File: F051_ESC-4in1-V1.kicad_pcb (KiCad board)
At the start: 4 copper layers, 46 x 49.5 mm, 204 parts, among them J1 Conn_01x02, J11 Conn_01x03, J14 Conn_01x03, J2 Conn_01x10, J3 Conn_01x05, J4 Conn_01x05, J5 Conn_01x05, J6 Conn_01x03, J7 Conn_01x05, J8 Conn_01x03, Q1 TPHR8504PL, Q10 TPHR8504PL, Q11 TPHR8504PL, Q12 TPHR8504PL, Q13 TPHR8504PL, Q14 TPHR8504PL, Q15 TPHR8504PL, Q16 TPHR8504PL, Q17 TPHR8504PL, Q18 TPHR8504PL, Q19 TPHR8504PL, Q2 TPHR8504PL, Q20 TPHR8504PL, Q21 TPHR8504PL, Q22 TPHR8504PL, Q23 TPHR8504PL, Q24 TPHR8504PL, Q3 TPHR8504PL, Q4 TPHR8504PL, Q5 TPHR8504PL, Q6 TPHR8504PL, Q7 TPHR8504PL, Q8 TPHR8504PL, Q9 TPHR8504PL, U1 STM32F051K6Ux, U10 FD6288Q, U11 STM32F051K6Ux, U12 FD6288Q, U2 FD6288Q, U3 L78L12_SOT89, U4 LP2985-3.3, U5 INA139, U6 FD6288Q, U7 OPA340NA, U8 STM32F051K6Ux, U9 STM32F051K6Ux

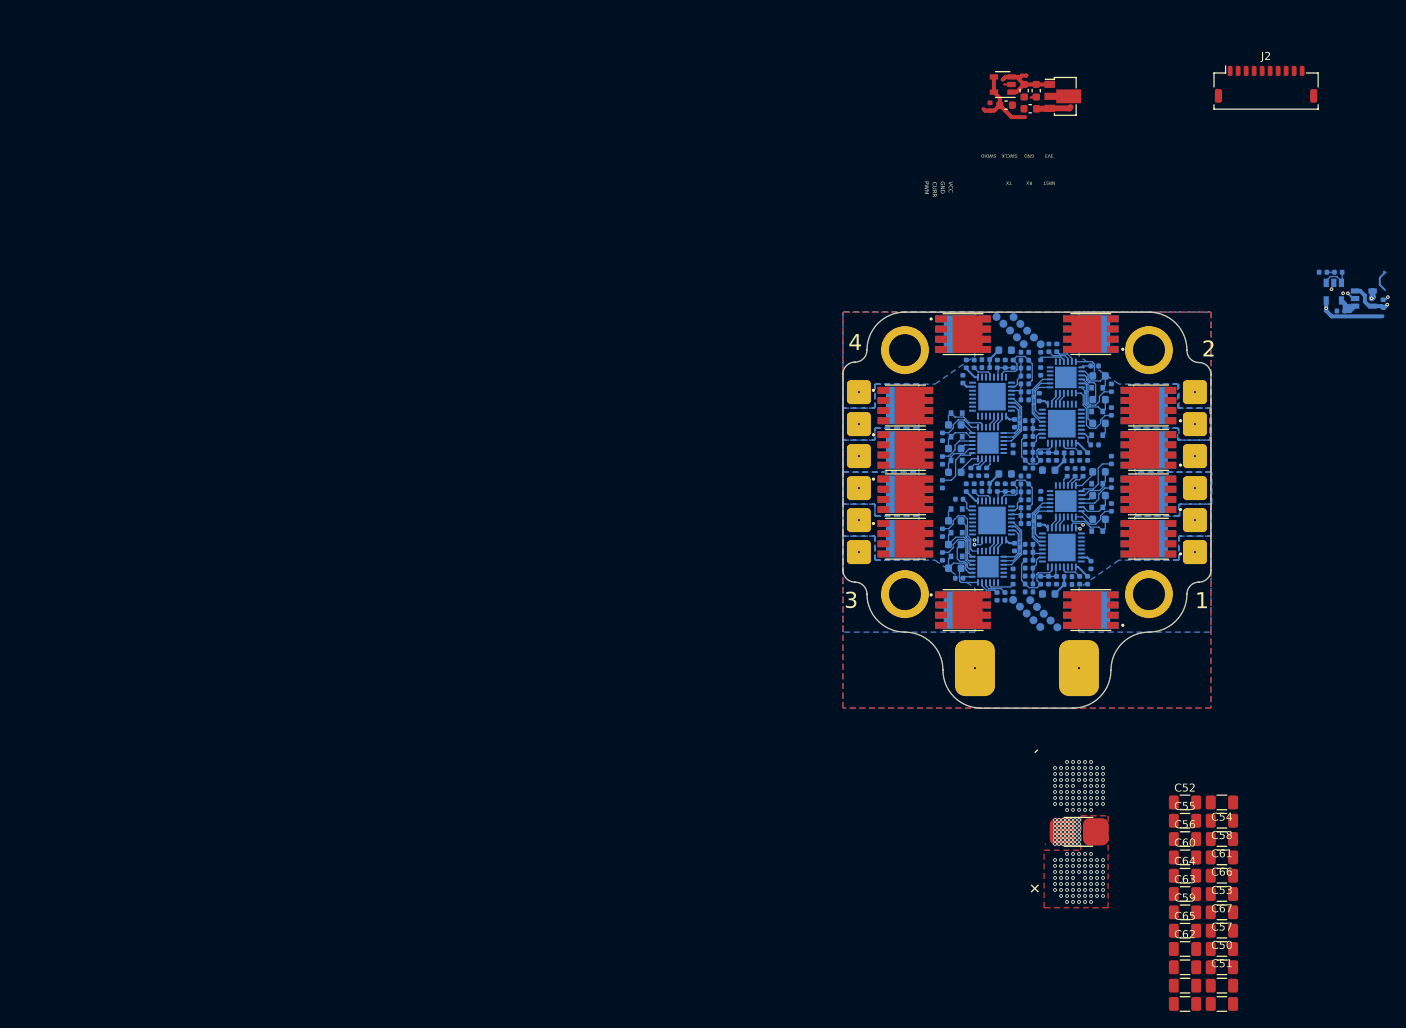
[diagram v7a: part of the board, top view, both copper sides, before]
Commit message: Addition of 5V Regulator
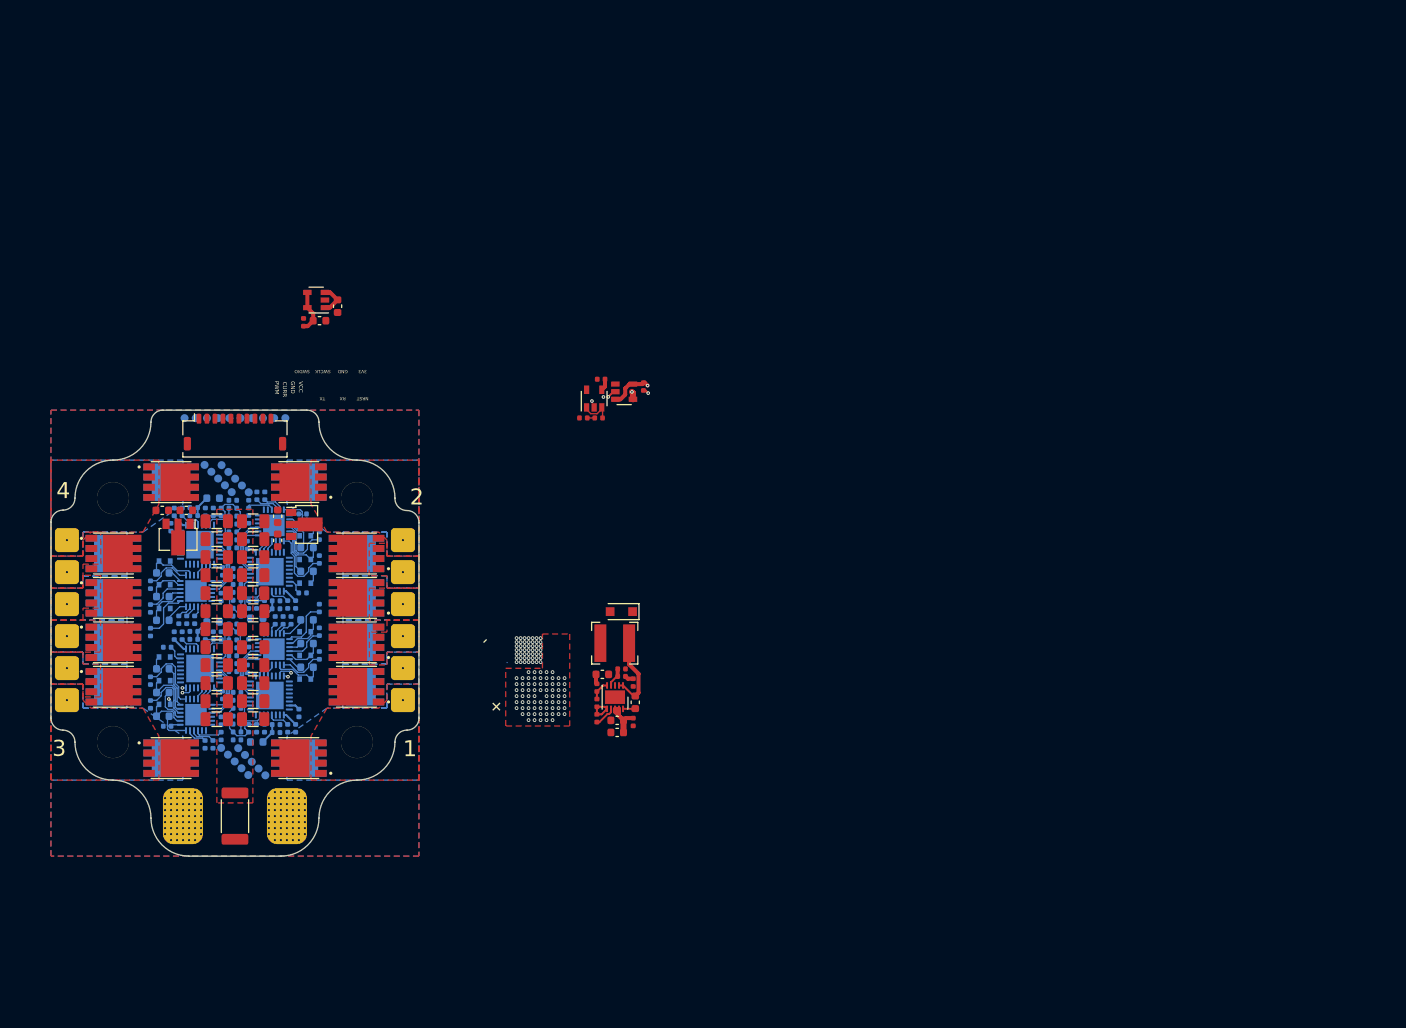
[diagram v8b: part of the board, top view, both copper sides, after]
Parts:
- added C68: 0.33uF, Capacitor_SMD:C_0603_1608Metric, F.Cu at (130.9, 74.8)
- added C69: 0.1uF, Capacitor_SMD:C_0603_1608Metric, F.Cu at (133.9, 74.8)
- added C70: 0.1uF, Capacitor_SMD:C_0603_1608Metric, F.Cu at (190.0, 98.8)
- added C71: 22uF, Capacitor_SMD:C_0603_1608Metric, F.Cu at (185.9, 95.3)
- added C72: 2.2uF, Capacitor_SMD:C_0603_1608Metric, F.Cu at (187.8, 102.5)
- added C73: 2.2uF, Capacitor_SMD:C_0603_1608Metric, F.Cu at (187.8, 101.0)
- added C74: 0.1uF, Capacitor_SMD:C_0402_1005Metric, F.Cu at (189.8, 101.2)
- added C75: 560pF, Capacitor_SMD:C_0402_1005Metric, F.Cu at (188.3, 95.5)
- added C76: 2pF, Capacitor_SMD:C_0402_1005Metric, F.Cu at (188.3, 94.6)
- added D13: 50V, 2A, Diode_SMD:D_SOD-123F, F.Cu at (188.3, 87.4)
- added J9: Conn_01x10, Connector_Wire:Conn_FC_Solder_10, B.Cu at (140.0, 63.2)
- added L1: L_Small, Inductor_SMD:L_Bourns-SRN5020, F.Cu at (187.5, 91.4)
- added R73: 20k, Resistor_SMD:R_0402_1005Metric, F.Cu at (185.2, 96.9)
- added R74: 3.8k, Resistor_SMD:R_0402_1005Metric, F.Cu at (185.2, 98.8)
- added R76: 200k, Resistor_SMD:R_0402_1005Metric, F.Cu at (185.2, 100.8)
- added R77: 68k, Resistor_SMD:R_0402_1005Metric, F.Cu at (189.8, 96.3)
- added U13: L78L12_SOT89, Package_TO_SOT_SMD:SOT-89-3, F.Cu at (132.9, 78.1)
- added U14: MP4560_QFN10, Package_DFN_QFN:DFN-10-1EP_3x3mm_P0.5mm_EP1.7x2.5mm, F.Cu at (187.5, 98.1)
- C7, C8, R2, R3, U5, U7: moved to F.Cu
- H1, H2, H3, H4: footprint MountingHole:MountingHole_2.7mm_Pad -> MountingHole:MountingHole_4in1ESC
- R1: value 1m -> 0m30; footprint Footprints:SCMM2512S5-R001F -> Resistor_SMD:R_2512_6332Metric
- moved J2 136.0 mm to (140.0, 65.0)
- moved C17 126.2 mm to (142.3, 100.9)
- moved C19 126.2 mm to (142.3, 98.6)
- moved C21 126.2 mm to (142.3, 96.4)
- moved C51 126.2 mm to (142.3, 94.1)
- moved C50 126.2 mm to (142.3, 91.9)
- moved C16 126.2 mm to (137.7, 100.9)
- moved C57 126.2 mm to (142.3, 89.6)
- moved C18 126.2 mm to (137.7, 98.6)
- moved C67 126.1 mm to (142.3, 87.4)
- moved C20 126.1 mm to (137.7, 96.4)
- moved C53 126.1 mm to (142.3, 85.1)
- moved C62 126.1 mm to (137.7, 94.1)
- moved C66 126.1 mm to (142.3, 82.9)
- moved C65 126.1 mm to (137.7, 91.9)
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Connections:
- C22 pad 1: +12V -> +5V
- J2 pad 3: (no net) -> +5V
- U4 pad 1: +12V -> +5V
- U4 pad 3: +12V -> +5V
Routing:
- net +3V3: track 31.6 -> 18.2 mm, vias 1 -> 0
- net Net-(C70-Pad1): track 0.00 -> 9.84 mm
- net +12V: track 9.68 -> 0.76 mm, vias 0 -> 1
- net +5V: track 0.00 -> 5.17 mm
- net Net-(R2-Pad1): track 5.74 -> 1.49 mm
- net +3.3VA: track 13.4 -> 10.6 mm
- net Net-(R76-Pad1): track 0.00 -> 2.70 mm
- net VCC_Shunt: track 5.32 -> 7.87 mm
- net Net-(R73-Pad2): track 0.00 -> 2.53 mm
- net Net-(C75-Pad1): track 0.00 -> 2.48 mm
- net GND: track 3.56 -> 5.75 mm, vias 75 -> 61
- net Net-(C70-Pad2): track 0.00 -> 1.54 mm
- net Net-(C75-Pad2): track 0.00 -> 1.08 mm
- net VCC: vias 72 -> 130
- added copper zone on In2.Cu, net +12V
- added copper zone on F.Cu, net /MCU 1/PhaseA
- added copper zone on F.Cu, net /MCU 1/PhaseC
- added copper zone on F.Cu, net /MCU 2/PhaseA
- added copper zone on F.Cu, net /MCU 2/PhaseB
- added copper zone on F.Cu, net /MCU 2/PhaseC
- added copper zone on F.Cu, net /MCU 3/PhaseA
- added copper zone on F.Cu, net /MCU 3/PhaseB
- added copper zone on F.Cu, net /MCU 3/PhaseC
- added copper zone on F.Cu, net /MCU 4/PhaseA
- added copper zone on F.Cu, net /MCU 4/PhaseB
- added copper zone on F.Cu, net /MCU 4/PhaseC
- added copper zone on F.Cu, net VCC_Shunt
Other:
- board size 46 x 49.5 mm -> 46 x 55.8 mm
